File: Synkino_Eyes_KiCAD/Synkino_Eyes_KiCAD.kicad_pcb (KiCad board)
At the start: 2 copper layers, 8.1 x 13 mm, 7 parts, among them J1 EYE1_OUT, U1 QRE1113GR

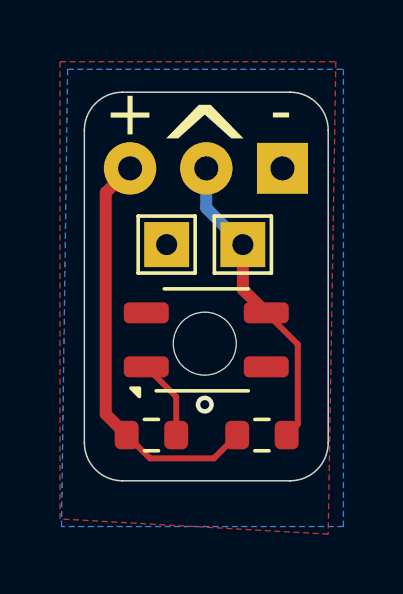
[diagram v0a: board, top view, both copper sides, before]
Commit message: Panelized Eyes separated from main Board, allowing V-Cuts
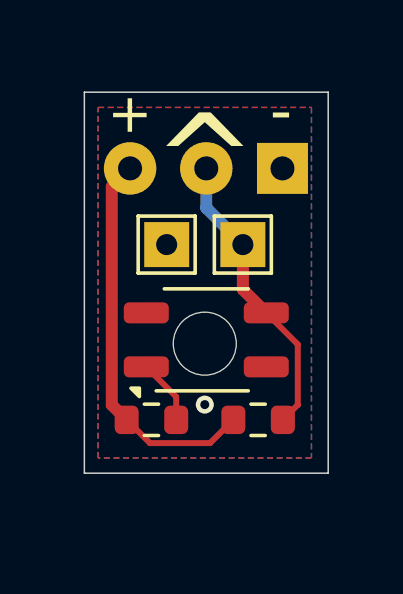
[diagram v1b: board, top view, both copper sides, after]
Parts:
- REF**: value MountingHole_2.1mm_just_hole -> O
- moved R2 0.52 mm to (93.2, 84.6)
- moved R1 0.51 mm to (89.7, 84.6)
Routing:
- net Net-(J1-Pin_3): track 13.8 -> 13.0 mm
- net Net-(U1-A): track 2.69 -> 2.18 mm
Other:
- board size 8.1 x 13 mm -> 8.1 x 12.7 mm
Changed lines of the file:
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@@
 			(at 0 1.75 0)
 			(layer "F.Fab")
+			(hide yes)
 			(effects
 				(font
@@
 			(at 0 3.9 -90)
 			(layer "F.Fab")
+			(hide yes)
 			(effects
 				(font
@@
 			)
 		)
-		(property "Value" "MountingHole_2.1mm_just_hole"
+		(property "Value" "O"
 			(at 0 3.2 0)
 			(layer "F.Fab")
+			(hide yes)
 			(effects
 				(font
@@
 			(at 0 1.75 0)
 			(layer "F.Fab")
+			(hide yes)
 			(effects
 				(font
@@
 	(footprint "Resistor_SMD:R_0603_1608Metric"
 		(layer "F.Cu")
-		(at 89.662 85.09)
+		(at 89.662 84.582)
 		(descr "Resistor SMD 0603 (1608 Metric), square (rectangular) end terminal, IPC_7351 nominal, (Body size source: IPC-SM-782 page 72, https://www.pcb-3d.com/wordpress/wp-content/uploads/ipc-sm-782a_amendment_1_and_2.pdf), generated with kicad-footprint-generator")
 		(tags "resistor")
@@
 			(at 0 1.43 0)
 			(layer "F.Fab")
+			(hide yes)
 			(effects
 				(font
@@
 	(footprint "Resistor_SMD:R_0603_1608Metric"
 		(layer "F.Cu")
-		(at 93.345 85.09)
+		(at 93.218 84.582)
 		(descr "Resistor SMD 0603 (1608 Metric), square (rectangular) end terminal, IPC_7351 nominal, (Body size source: IPC-SM-782 page 72, https://www.pcb-3d.com/wordpress/wp-content/uploads/ipc-sm-782a_amendment_1_and_2.pdf), generated with kicad-footprint-generator")
 		(tags "resistor")
@@
 			(at 0 1.43 0)
 			(layer "F.Fab")
+			(hide yes)
 			(effects
 				(font
@@
 		)
 	)
-	(gr_arc
-		(start 95.554 85.344)
-		(mid 95.182026 86.242026)
-		(end 94.284 86.614)
+	(gr_line
+		(start 95.554 73.66)
+		(end 95.554 86.36)
+		(stroke
+			(width 0.05)
+			(type solid)
+		)
+		(layer "Edge.Cuts")
+	)
+	(gr_line
+		(start 87.426 86.36)
+		(end 95.554 86.36)
 		(stroke
 			(width 0.05)
@@
 		(layer "Edge.Cuts")
 	)
-	(gr_arc
-		(start 87.426 74.93)
-		(mid 87.797974 74.031974)
-		(end 88.696 73.66)
-		(stroke
-			(width 0.05)
-			(type default)
-		)
-		(layer "Edge.Cuts")
-	)
 	(gr_line
-		(start 95.554 74.93)
-		(end 95.554 85.344)
+		(start 87.426 73.66)
+		(end 87.426 86.36)
 		(stroke
 			(width 0.05)
@@
 	)
 	(gr_line
-		(start 88.696 86.614)
-		(end 94.284 86.614)
-		(stroke
-			(width 0.05)
-			(type default)
-		)
-		(layer "Edge.Cuts")
-	)
-	(gr_line
-		(start 87.426 74.93)
-		(end 87.426 85.344)
-		(stroke
-			(width 0.05)
-			(type solid)
-		)
-		(layer "Edge.Cuts")
-	)
-	(gr_arc
-		(start 88.696 86.614)
-		(mid 87.797974 86.242026)
-		(end 87.426 85.344)
-		(stroke
-			(width 0.05)
-			(type default)
-		)
-		(layer "Edge.Cuts")
-	)
-	(gr_line
-		(start 88.696 73.66)
-		(end 94.284 73.66)
-		(stroke
-			(width 0.05)
-			(type default)
-		)
-		(layer "Edge.Cuts")
-	)
-	(gr_arc
-		(start 94.284 73.66)
-		(mid 95.182026 74.031974)
-		(end 95.554 74.93)
+		(start 87.426 73.66)
+		(end 95.554 73.66)
 		(stroke
 			(width 0.05)
@@
 	)
 	(gr_text "^"
-		(at 91.44 75.692 0)
+		(at 91.44 75.946 0)
 		(layer "F.SilkS")
 		(effects
@@
 		(effects
 			(font
-				(size 1.5 1.5)
+				(size 1.3 1.3)
 				(thickness 0.15)
 			)
@@
 	)
 	(segment
+		(start 88.837 84.582)
+		(end 89.612 85.357)
+		(width 0.2)
+		(layer "F.Cu")
+		(net 2)
+	)
+	(segment
+		(start 89.612 85.357)
+		(end 91.618 85.357)
+		(width 0.2)
+		(layer "F.Cu")
+		(net 2)
+	)
+	(segment
+		(start 88.34 84.085)
+		(end 88.837 84.582)
+		(width 0.4)
+		(layer "F.Cu")
+		(net 2)
+	)
+	(segment
 		(start 88.95 76.2)
-		(end 88.138 77.012)
+		(end 88.34 76.81)
 		(width 0.4)
 		(layer "F.Cu")
@@
 	)
 	(segment
-		(start 88.138 77.012)
-		(end 88.138 84.391)
+		(start 88.34 76.81)
+		(end 88.34 84.085)
 		(width 0.4)
 		(layer "F.Cu")
@@
 	)
 	(segment
-		(start 91.745 85.865)
-		(end 92.52 85.09)
+		(start 91.618 85.357)
+		(end 92.393 84.582)
 		(width 0.2)
 		(layer "F.Cu")
@@
 	)
 	(segment
-		(start 89.612 85.865)
-		(end 91.745 85.865)
-		(width 0.2)
-		(layer "F.Cu")
-		(net 2)
-	)
-	(segment
-		(start 88.138 84.391)
-		(end 88.837 85.09)
+		(start 92.71 80.235)
+		(end 92.71 78.74)
 		(width 0.4)
-		(layer "F.Cu")
-		(net 2)
-	)
-	(segment
-		(start 88.837 85.09)
-		(end 89.612 85.865)
-		(width 0.2)
-		(layer "F.Cu")
-		(net 2)
-	)
-	(segment
-		(start 94.17 85.09)
-		(end 94.54 84.72)
-		(width 0.2)
-		(layer "F.Cu")
-		(net 3)
-	)
-	(segment
-		(start 94.54 84.72)
-		(end 94.54 82.065)
-		(width 0.2)
 		(layer "F.Cu")
 		(net 3)
@@
 	)
 	(segment
-		(start 92.71 80.235)
-		(end 92.71 78.74)
-		(width 0.4)
-		(layer "F.Cu")
-		(net 3)
-	)
-	(segment
 		(start 93.49 81.015)
 		(end 92.71 80.235)
 		(width 0.4)
+		(layer "F.Cu")
+		(net 3)
+	)
+	(segment
+		(start 94.54 84.085)
+		(end 94.54 82.065)
+		(width 0.2)
+		(layer "F.Cu")
+		(net 3)
+	)
+	(segment
+		(start 94.043 84.582)
+		(end 94.54 84.085)
+		(width 0.2)
 		(layer "F.Cu")
 		(net 3)
@@
 	)
 	(segment
-		(start 90.487 83.812)
-		(end 90.487 85.09)
-		(width 0.2)
-		(layer "F.Cu")
-		(net 4)
-	)
-	(segment
 		(start 89.49 82.815)
 		(end 90.487 83.812)
+		(width 0.2)
+		(layer "F.Cu")
+		(net 4)
+	)
+	(segment
+		(start 90.487 83.812)
+		(end 90.487 84.582)
 		(width 0.2)
 		(layer "F.Cu")
@@
 		(polygon
 			(pts
-				(xy 86.614 72.644) (xy 95.808 72.644) (xy 95.554 88.392) (xy 86.614 87.884)
+				(xy 87.884 74.168) (xy 94.996 74.168) (xy 94.996 85.852) (xy 87.884 85.852)
 			)
 		)
@@
 		(polygon
 			(pts
-				(xy 86.868 72.898) (xy 96.062 72.898) (xy 96.062 88.138) (xy 86.664 88.138)
-			)
-		)
-	)
-	(group ""
-		(members "089fca26-8a12-4f87-bbe7-2cbc6ab60e55" "64edfb76-16df-483c-bead-1e4dee4d29b6"
-			"9c3a36f6-094d-4207-bef9-3c39089e7bad"
-		)
-	)
+				(xy 87.884 74.168) (xy 94.996 74.168) (xy 94.996 85.852) (xy 87.884 85.852)
+			)
+		)
+	)
